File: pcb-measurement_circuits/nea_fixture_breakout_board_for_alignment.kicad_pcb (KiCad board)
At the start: 2 copper layers, 60 x 40 mm, 33 parts, among them P1 CONN_02X13, P2 CONN_02X15, U1 MS8607

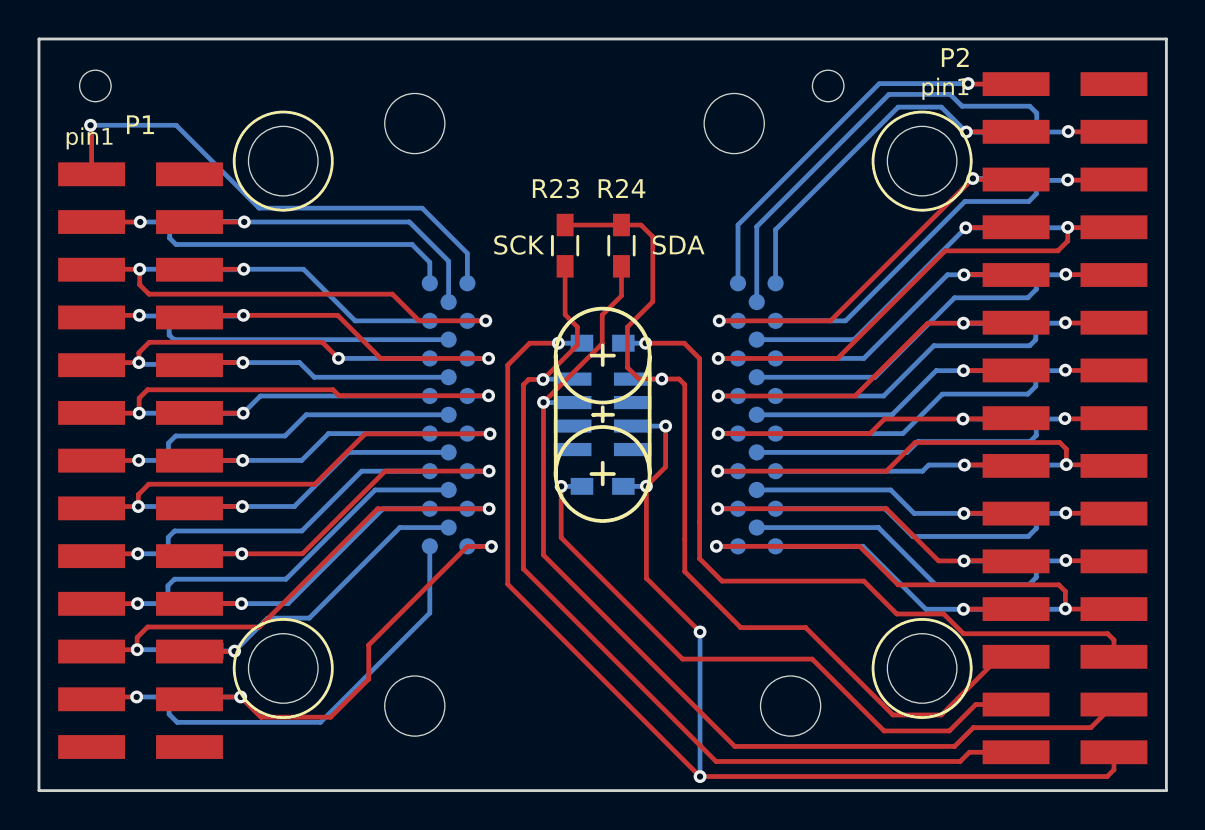
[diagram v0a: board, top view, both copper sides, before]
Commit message: --fixed breakout pcb drill file for reorder and regenerated gerbers --
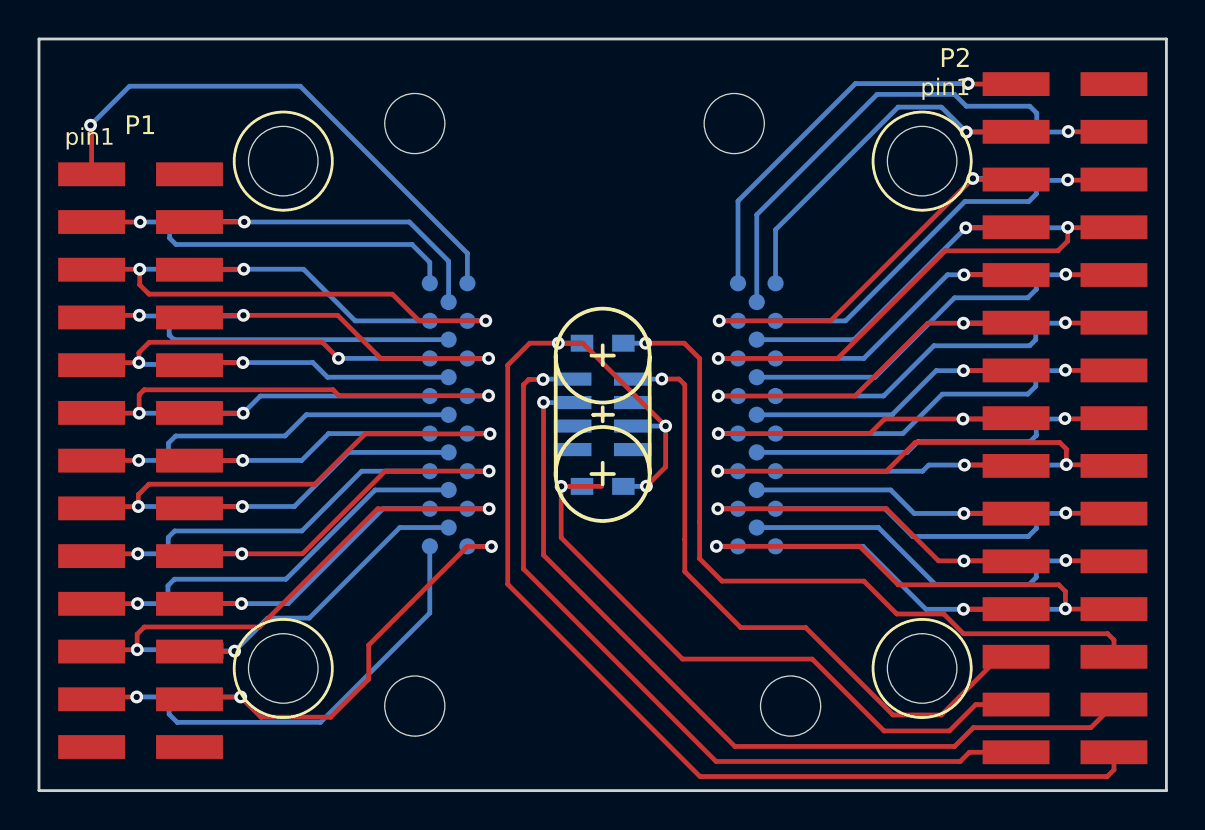
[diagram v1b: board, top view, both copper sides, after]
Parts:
- removed H3: dowel_holes2, footprints_on_Cdrive:dowel_holes2
- removed R23, R24: 10k, Resistors_SMD:R_0603_HandSoldering
- R10: value 6.81k -> 10k
- R11: value 7.5k -> 10k
- R12: value 8.2k -> 10k
- R14: value 11k -> 10k
- R15: value 12k -> 10k
- R16: value 13k -> 10k
- R17: value 14k -> 10k
- R18: value 15k -> 10k
- R19: value 16k -> 10k
- R2: value 1.5k -> 10k
- R20: value 17.4k -> 10k
- R21: value 18k -> 10k
- R22: value 20k -> 10k
- R3: value 2k -> 10k
- R4: value 2.7k -> 10k
- R5: value 3.3k -> 10k
- R6: value 3.9k -> 10k
- R7: value 4.7k -> 10k
- R8: value 5.6k -> 10k
- R9: value 6.2k -> 10k
- moved P2 18.0 mm to (24.6, 0.18)
- moved P1 15.5 mm to (-24.6, 2.44)
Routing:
- net /VDD: track 49.4 -> 34.9 mm
- net GND: track 76.9 -> 67.8 mm, vias 5 -> 3
- net /SDA: track 54.1 -> 45.2 mm
- net /SCL: track 50.3 -> 43.2 mm
- net /LED1: track 32.9 -> 35.1 mm
- net /MID1: track 27.1 -> 28.8 mm
- net /MID2: track 21.0 -> 21.8 mm
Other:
- board text removed: "SCK"
- board text removed: "SDA"
